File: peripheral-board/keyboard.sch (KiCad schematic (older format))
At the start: 142 parts

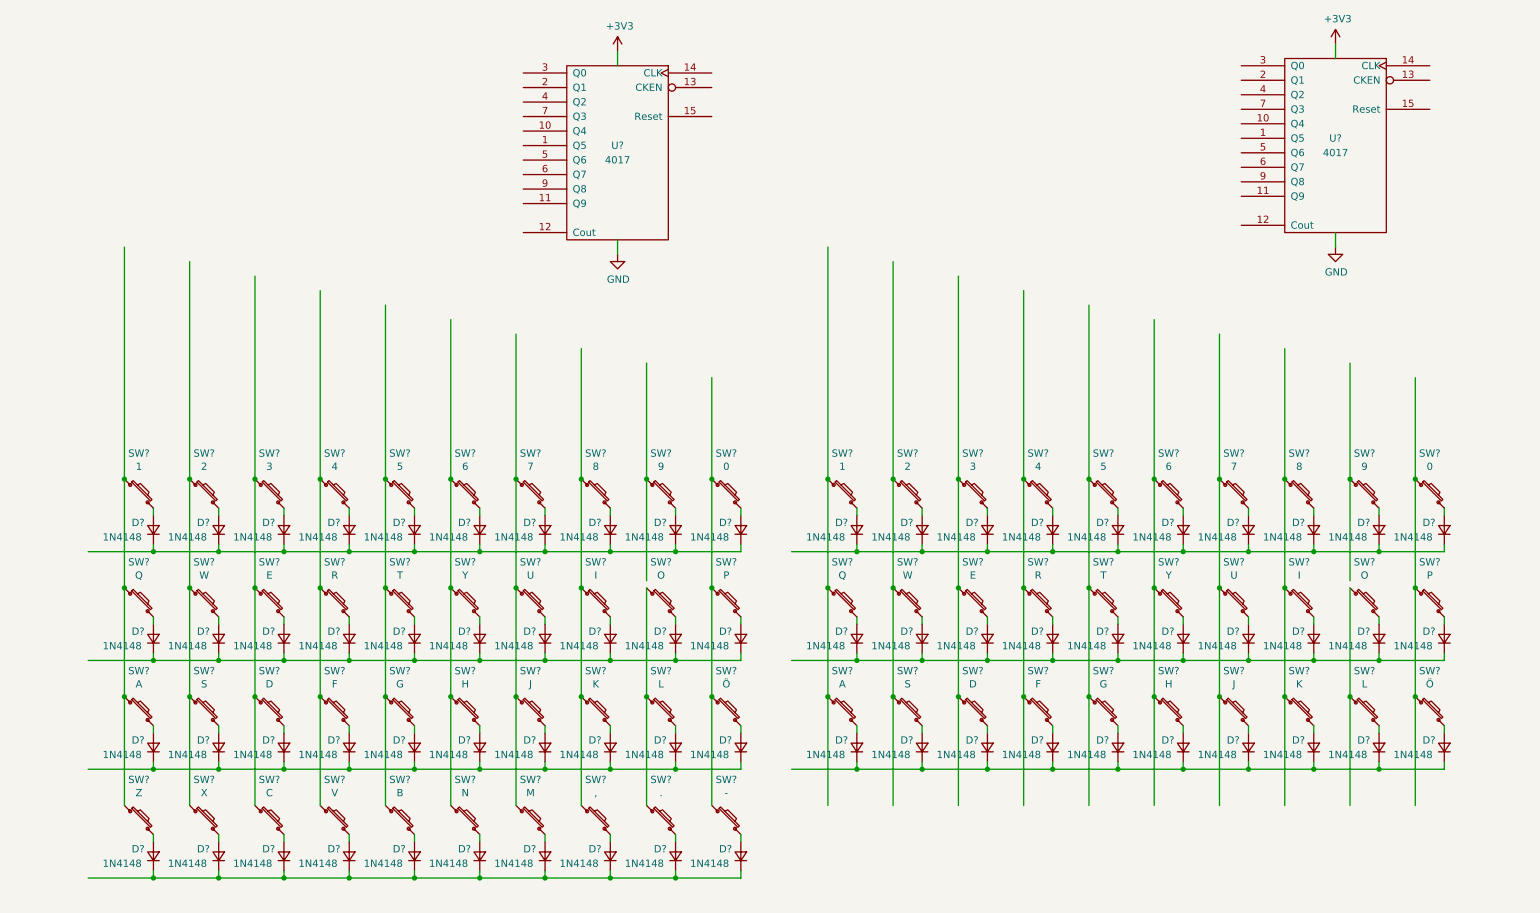
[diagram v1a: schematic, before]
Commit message: added button 3d model
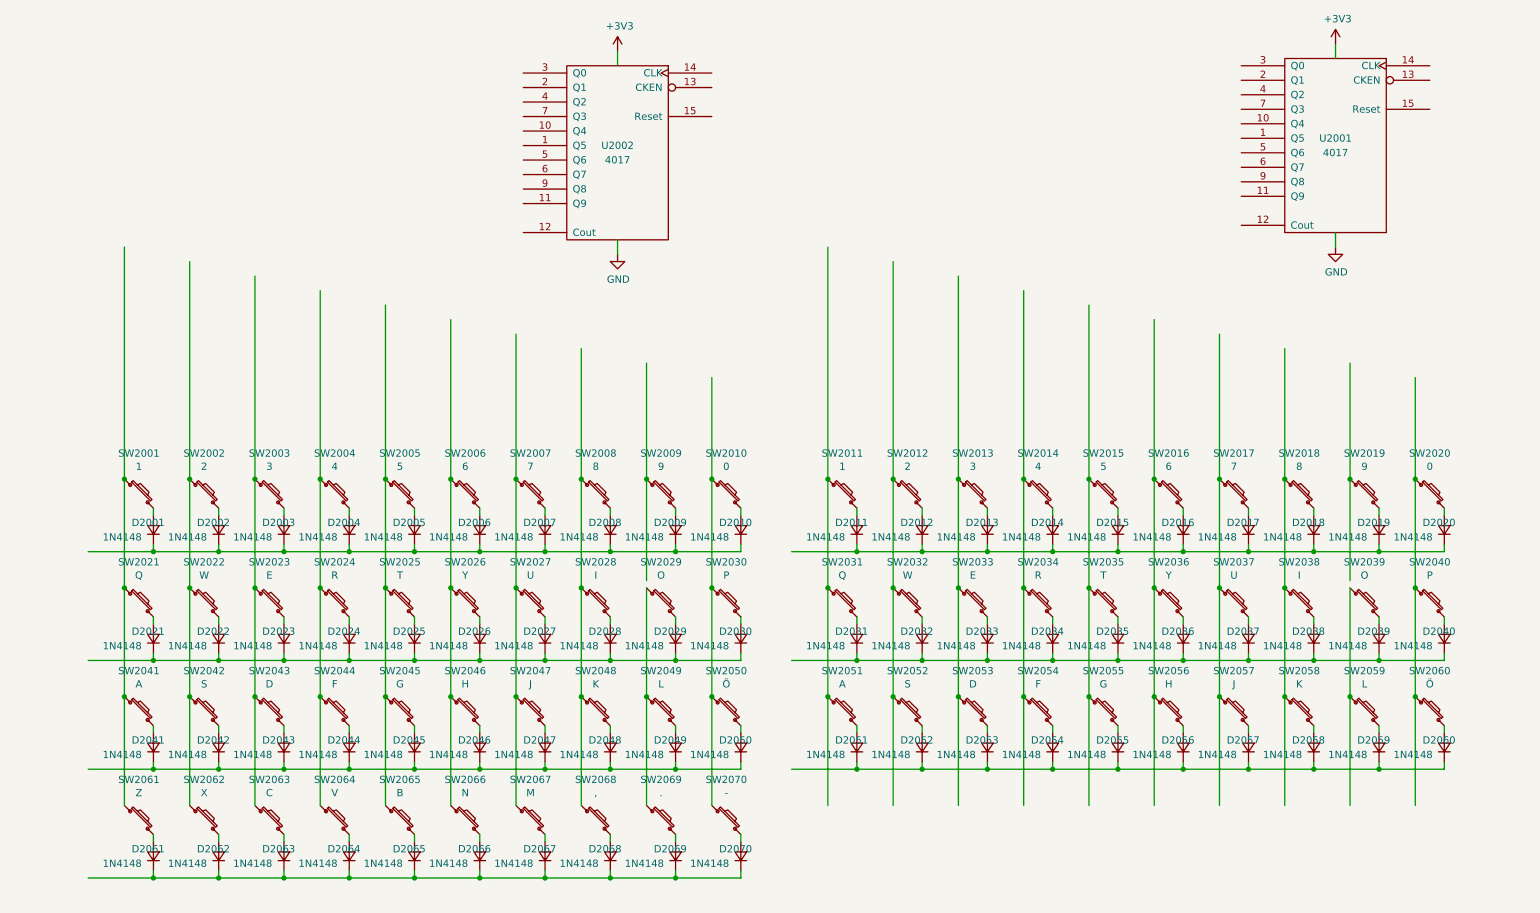
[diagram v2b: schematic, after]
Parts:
- D2001, D2002, D2003, D2004, D2005, D2006, D2007, D2008, D2009, D2010, D2011, D2012, D2013, D2014, D2015, D2016, D2017, D2018, D2019, D2020, D2021, D2022, D2023, D2024, D2025, D2026, D2027, D2028, D2029, D2030, D2031, D2032, D2033, D2034, D2035, D2036, D2037, D2038, D2039, D2040, D2041, D2042, D2043, D2044, D2045, D2046, D2047, D2048, D2049, D2050, D2051, D2052, D2053, D2054, D2055, D2056, D2057, D2058, D2059, D2060, D2061, D2062, D2063, D2064, D2065, D2066, D2067, D2068, D2069, D2070: renamed from D?; footprint (none) -> Diodes_SMD:MiniMELF_Standard
- SW2001, SW2002, SW2003, SW2004, SW2005, SW2006, SW2007, SW2008, SW2009, SW2010, SW2011, SW2012, SW2013, SW2014, SW2015, SW2016, SW2017, SW2018, SW2019, SW2020, SW2021, SW2022, SW2023, SW2024, SW2025, SW2026, SW2027, SW2028, SW2029, SW2030, SW2031, SW2032, SW2033, SW2034, SW2035, SW2036, SW2037, SW2038, SW2039, SW2040, SW2041, SW2042, SW2043, SW2044, SW2045, SW2046, SW2047, SW2048, SW2049, SW2050, SW2051, SW2052, SW2053, SW2054, SW2055, SW2056, SW2057, SW2058, SW2059, SW2060, SW2061, SW2062, SW2063, SW2064, SW2065, SW2066, SW2067, SW2068, SW2069, SW2070: renamed from SW?; footprint (none) -> lib:SMD-TACT-5.2x5.2x2mm
- gave numbers to parts that had none: 2

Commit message: added keyboard scanning logic
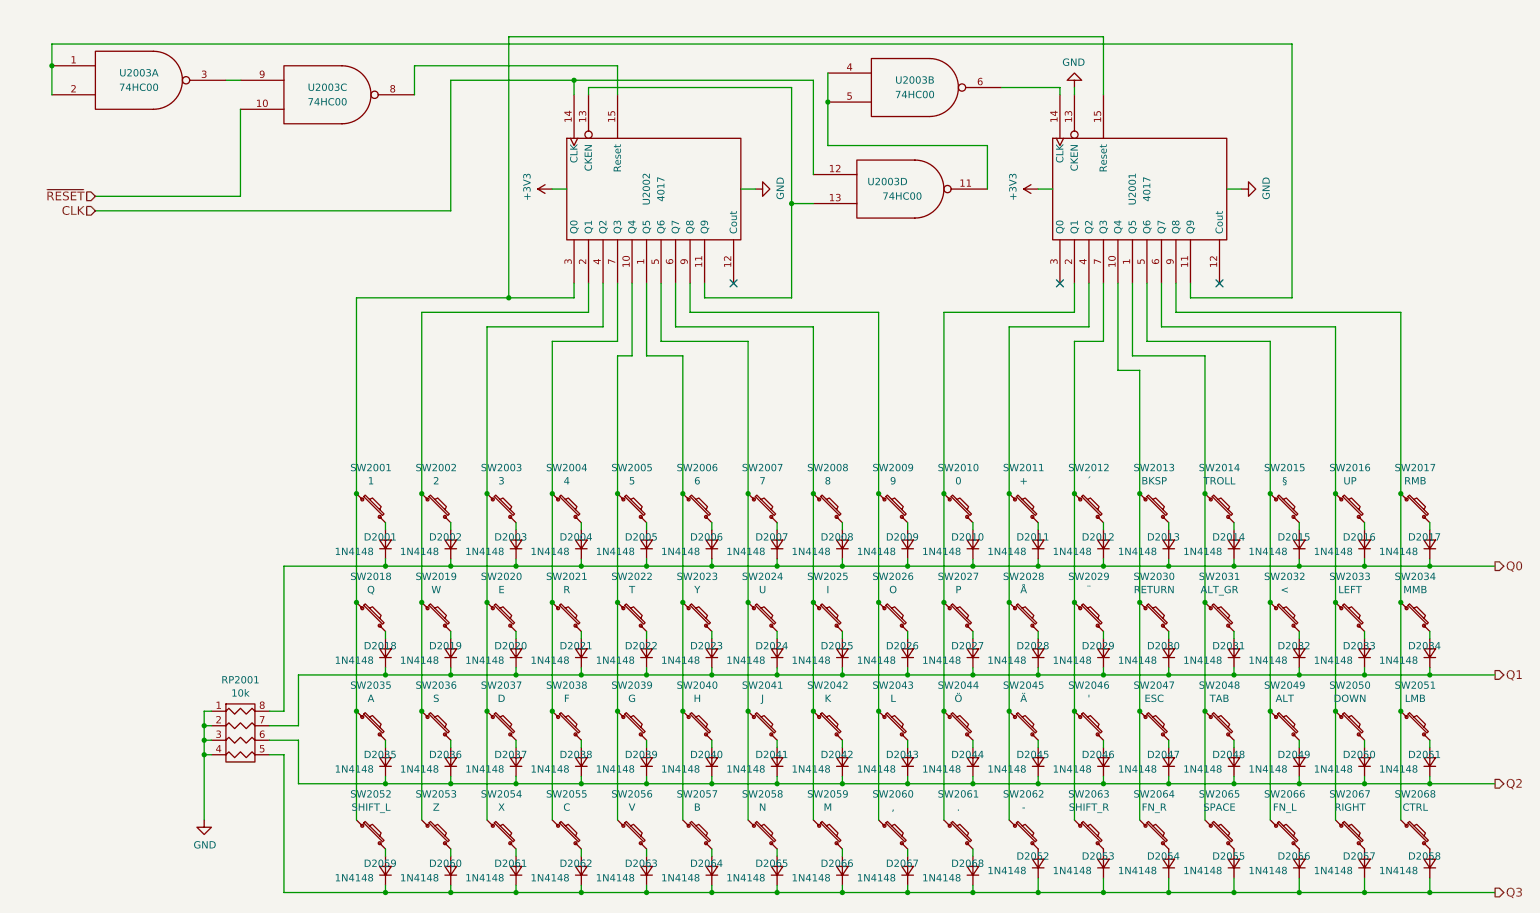
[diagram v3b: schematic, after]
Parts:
- removed D2018, D2019, D2020, D2038, D2039, D2040, D2059, D2060: 1N4148, Diodes_SMD:MiniMELF_Standard, symbol D_Small
- removed SW2018: 8, lib:SMD-TACT-5.2x5.2x2mm, symbol SW_PUSH_Small
- removed SW2019: 9, lib:SMD-TACT-5.2x5.2x2mm, symbol SW_PUSH_Small
- removed SW2038: I, lib:SMD-TACT-5.2x5.2x2mm, symbol SW_PUSH_Small
- removed SW2039: O, lib:SMD-TACT-5.2x5.2x2mm, symbol SW_PUSH_Small
- removed SW2040: P, lib:SMD-TACT-5.2x5.2x2mm, symbol SW_PUSH_Small
- removed SW2058: K, lib:SMD-TACT-5.2x5.2x2mm, symbol SW_PUSH_Small
- removed SW2059: L, lib:SMD-TACT-5.2x5.2x2mm, symbol SW_PUSH_Small
- removed SW2060: Ö, lib:SMD-TACT-5.2x5.2x2mm, symbol SW_PUSH_Small
- added D2052, D2053, D2054, D2055, D2056, D2057: 1N4148, Diodes_SMD:MiniMELF_Standard, symbol D_Small
- added RP2001: 10k, Resistors_SMD:R_Cat16-4, symbol R_PACK4
- added SW2063: SHIFT_R, lib:SMD-TACT-5.2x5.2x2mm, symbol SW_PUSH_Small
- added SW2064: FN_R, lib:SMD-TACT-5.2x5.2x2mm, symbol SW_PUSH_Small
- added SW2065: SPACE, lib:SMD-TACT-5.2x5.2x2mm, symbol SW_PUSH_Small
- added SW2066: FN_L, lib:SMD-TACT-5.2x5.2x2mm, symbol SW_PUSH_Small
- added SW2067: RIGHT, lib:SMD-TACT-5.2x5.2x2mm, symbol SW_PUSH_Small
- added SW2068: CTRL, lib:SMD-TACT-5.2x5.2x2mm, symbol SW_PUSH_Small
- added U2003: 74HC00, Housings_SOIC:SOIC-14_3.9x8.7mm_Pitch1.27mm, symbol 74HC00
- SW2011: value 1 -> +
- SW2012: value 2 -> ´
- SW2013: value 3 -> BKSP
- SW2014: value 4 -> TROLL
- SW2015: value 5 -> §
- SW2016: value 6 -> UP
- SW2017: value 7 -> RMB
- SW2028: renamed from SW2031; value Q -> Å
- SW2029: renamed from SW2032; value W -> ¨
- SW2030: renamed from SW2033; value E -> RETURN
- SW2031: renamed from SW2034; value R -> ALT_GR
- SW2032: renamed from SW2035; value T -> <
- SW2033: renamed from SW2036; value Y -> LEFT
- SW2034: renamed from SW2037; value U -> MMB
- SW2045: renamed from SW2051; value A -> Ä
- SW2046: renamed from SW2052; value S -> '
- SW2047: renamed from SW2053; value D -> ESC
- SW2048: renamed from SW2054; value F -> TAB
- SW2049: renamed from SW2055; value G -> ALT
- SW2050: renamed from SW2056; value H -> DOWN
- SW2051: renamed from SW2057; value J -> LMB
- SW2052: renamed from SW2020; value 0 -> SHIFT_L
- U2001, U2002: footprint (none) -> Housings_SOIC:SOIC-16_3.9x9.9mm_Pitch1.27mm
- renumbered D2021 to D2018, D2022 to D2019, D2023 to D2020, D2024 to D2021, D2025 to D2022, D2026 to D2023, D2027 to D2024, D2028 to D2025, D2029 to D2026, D2030 to D2027, D2031 to D2028, D2032 to D2029, D2033 to D2030, D2034 to D2031, D2035 to D2032, D2036 to D2033, D2037 to D2034, D2041 to D2035, D2042 to D2036, D2043 to D2037, D2044 to D2038, D2045 to D2039, D2046 to D2040, D2047 to D2041, D2048 to D2042, D2049 to D2043, D2050 to D2044, D2051 to D2045, D2052 to D2046, D2053 to D2047, D2054 to D2048, D2055 to D2049, D2056 to D2050, D2057 to D2051, D2061 to D2059, D2062 to D2060, D2063 to D2061, D2064 to D2062, D2065 to D2063, D2066 to D2064, D2067 to D2065, D2068 to D2066, D2069 to D2067, D2070 to D2068, SW2021 to SW2018, SW2022 to SW2019, SW2023 to SW2020, SW2024 to SW2021, SW2025 to SW2022, SW2026 to SW2023, SW2027 to SW2024, SW2028 to SW2025, SW2029 to SW2026, SW2030 to SW2027, SW2041 to SW2035, SW2042 to SW2036, SW2043 to SW2037, SW2044 to SW2038, SW2045 to SW2039, SW2046 to SW2040, SW2047 to SW2041, SW2048 to SW2042, SW2049 to SW2043, SW2050 to SW2044, SW2061 to SW2053, SW2062 to SW2054, SW2063 to SW2055, SW2064 to SW2056, SW2065 to SW2057, SW2066 to SW2058, SW2067 to SW2059, SW2068 to SW2060, SW2069 to SW2061, SW2070 to SW2062
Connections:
- net labels added: CLK, Q0, Q1, Q2, Q3, ~RESET
- wire segments 173 -> 232
- no-connect marks 0 -> 3
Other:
- moved on the sheet: D2001, D2002, D2003, D2004, D2005, D2006, D2007, D2008, D2009, D2010, D2011, D2012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

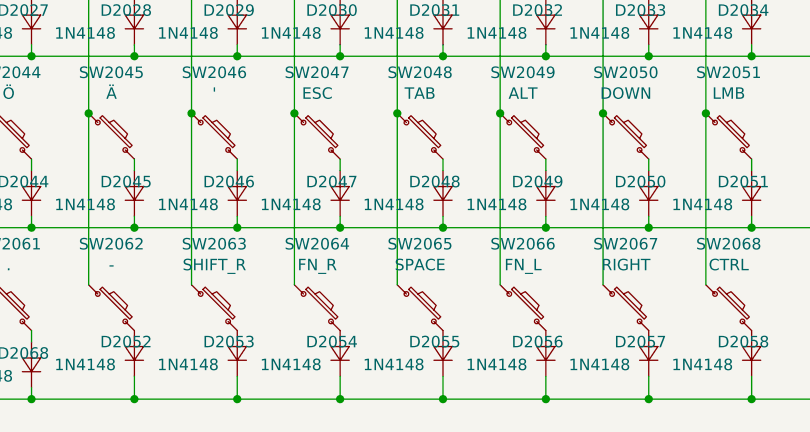
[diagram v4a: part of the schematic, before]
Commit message: keyboard switches and diodes placed
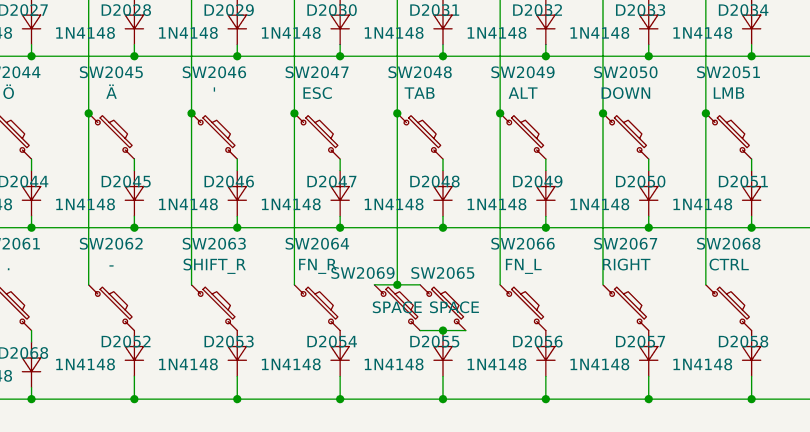
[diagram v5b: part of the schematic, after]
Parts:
- added SW2069: SPACE, lib:SMD-TACT-5.2x5.2x2mm, symbol SW_PUSH_Small
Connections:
- net at SW2014.1, SW2031.1, SW2048.1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: now also SW2069.1
- net at D2055.2 (A), SW2065.2: now also SW2069.2
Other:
- moved on the sheet: SW2065
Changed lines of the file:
@@
 LIBS:valves
 LIBS:amp
+LIBS:card-edge
 LIBS:peripheral-board-cache
 EELAYER 25 0
@@
 $Descr A4 11693 8268
 encoding utf-8
-Sheet 2 6
+Sheet 2 9
 Title ""
 Date ""
@@
 L SW_PUSH_Small SW2065
 U 1 1 581FB421
-P 8750 6050
-F 0 "SW2065" H 8750 6328 50  0000 C CNN
-F 1 "SPACE" H 8750 6237 50  0000 C CNN
-F 2 "lib:SMD-TACT-5.2x5.2x2mm" H 8750 6050 50  0001 C CNN
-F 3 "" H 8750 6050 50  0000 C CNN
-	1    8750 6050
+P 8850 6050
+F 0 "SW2065" H 8850 6200 50  0000 C CNN
+F 1 "SPACE" H 8900 6050 50  0000 C CNN
+F 2 "lib:SMD-TACT-5.2x5.2x2mm" H 8850 6050 50  0001 C CNN
+F 3 "" H 8850 6050 50  0000 C CNN
+	1    8850 6050
 	1    0    0    -1
 $EndComp
@@
 Wire Wire Line
 	2000 1650 2000 1050
+$Comp
+L SW_PUSH_Small SW2069
+U 1 1 581FB5B7
+P 8650 6050
+F 0 "SW2069" H 8500 6200 50  0000 C CNN
+F 1 "SPACE" H 8650 6050 50  0000 C CNN
+F 2 "lib:SMD-TACT-5.2x5.2x2mm" H 8650 6050 50  0001 C CNN
+F 3 "" H 8650 6050 50  0000 C CNN
+	1    8650 6050
+	1    0    0    -1
+$EndComp
+Wire Wire Line
+	8550 5950 8750 5950
+Connection ~ 8650 5950
+Wire Wire Line
+	8750 6150 8950 6150
+Connection ~ 8850 6150
 $EndSCHEMATC

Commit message: routed keyboard
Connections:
- net labels added: COL0, COL1, COL10, COL11, COL12, COL13, COL14, COL15, COL16, COL2, COL3, COL4, COL5, COL6, COL7, COL8, COL9, ROW0, ROW1, ROW2, ROW3
- wire segments 234 -> 236
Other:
- moved on the sheet: D2015, D2017, D2034, D2049, D2051, D2058, SW2015, SW2017, SW2034, SW2049, SW2051, SW2068

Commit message: some more keyboard stuff fit on this side..
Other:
- moved on the sheet: D2017, D2033, D2051, D2057, SW2017, SW2033, SW2051, SW2067
